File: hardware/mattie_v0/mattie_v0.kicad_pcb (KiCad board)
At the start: 4 copper layers, 55 x 32 mm, 53 parts, among them J1 5V, J2 USB_B_Mini, J3 Power, U1 STM32F40X_LQFP64, U2 ICE40UP5K-SG48ITR, U3 MCP1826T, U4 MCP1826S-3302, U5 DSC1004, Y1 8Mhz

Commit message: adding some cap
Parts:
- added C26: 0.1u, Capacitor_SMD:C_0603_1608Metric, F.Cu at (146.9, 124.0)
- 5 - 6V: renamed from J1
- renumbered BOOT_MODE to SW1
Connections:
- net /MCU/ADC12_IN8 renamed Net-(U1-Pad26)
- net /MCU/ADC12_IN9 renamed Net-(U1-Pad27)
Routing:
- net +1V2: track 75.2 -> 91.6 mm
- net GND: track 453.9 -> 450.6 mm

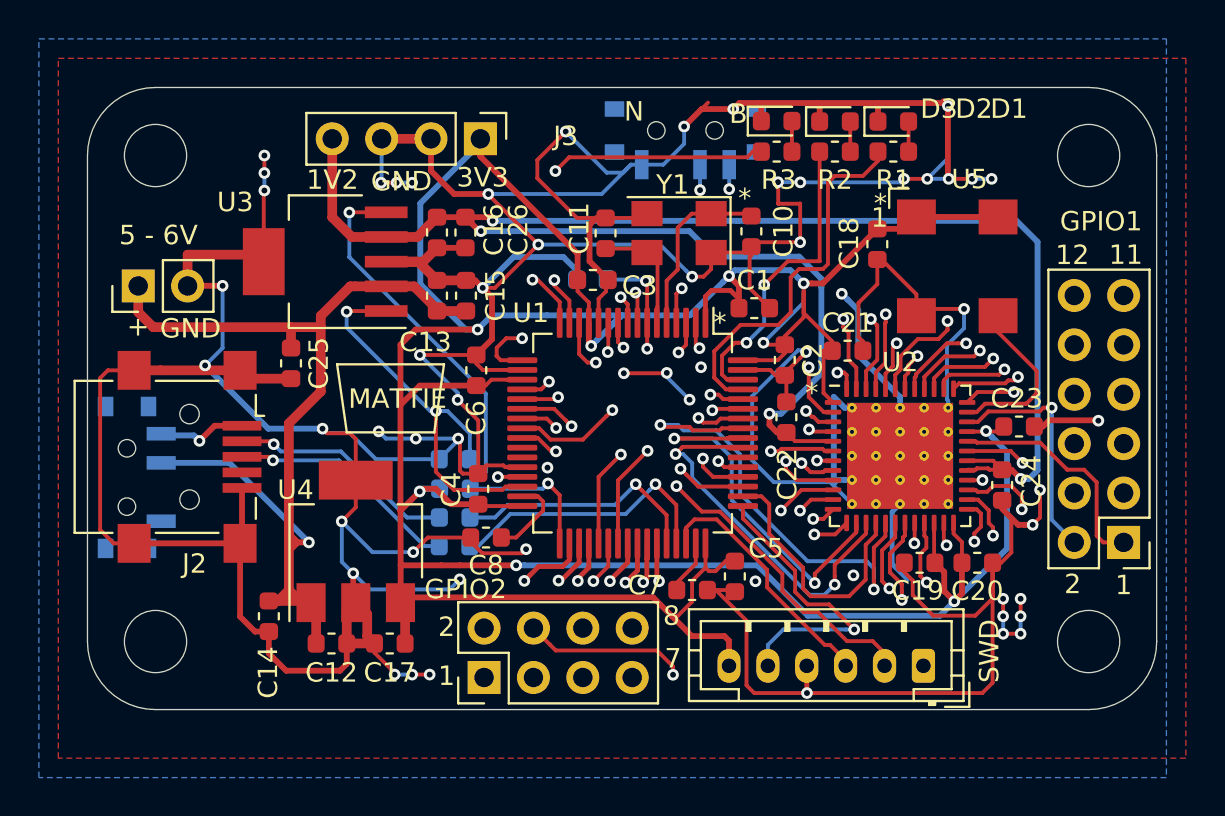
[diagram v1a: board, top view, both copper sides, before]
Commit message: added pullups and pulldowns
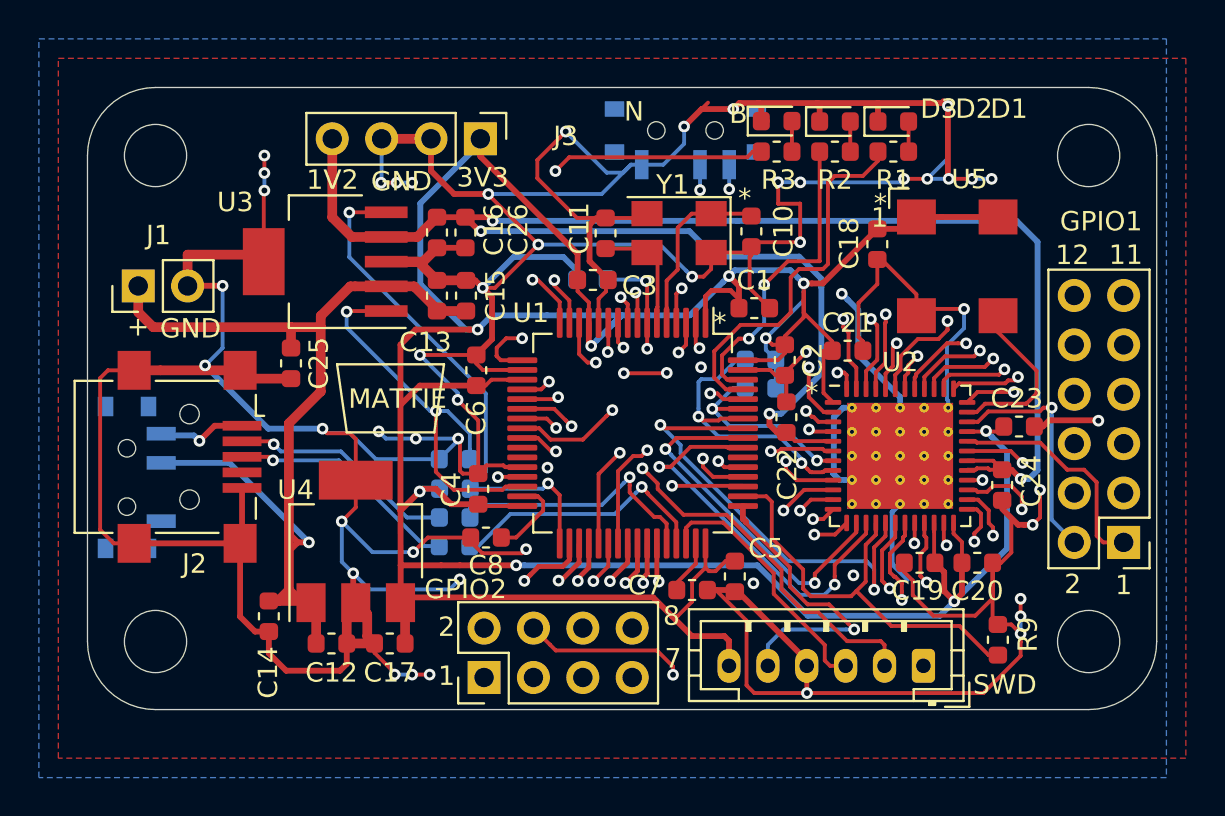
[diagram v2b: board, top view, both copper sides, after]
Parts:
- added R10: 10K, Resistor_SMD:R_0603_1608Metric, B.Cu at (162.1, 132.0)
- added R6: 10K, Resistor_SMD:R_0603_1608Metric, B.Cu at (162.1, 130.5)
- added R9: 10K, Resistor_SMD:R_0603_1608Metric, F.Cu at (174.3, 144.9)
- J1: renamed from 5 - 6V
- renumbered SW1 to BOOT_MODE
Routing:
- net GND: track 450.6 -> 439.9 mm, vias 55 -> 51
- net /LATTICE_ICE40/SPI_SS: track 13.5 -> 22.3 mm
- net /LATTICE_ICE40/RESET: track 10.7 -> 15.5 mm
- net +3V3: track 200.6 -> 203.1 mm
- net /LATTICE_ICE40/DONE: track 8.89 -> 11.0 mm
- net /LATTICE_ICE40/SPI_SCK: track 19.3 -> 20.6 mm
- net /LATTICE_ICE40/SPI_MOSI: track 24.4 -> 23.4 mm
- net Net-(R4-Pad1): track 12.9 -> 13.7 mm
- net Net-(R5-Pad1): track 14.4 -> 13.7 mm
- net /MCU/NRST: track 29.6 -> 30.2 mm
- net /MCU/SWCLK: track 15.4 -> 15.9 mm
- net /LATTICE_ICE40/DAT7: track 26.6 -> 26.1 mm

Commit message: Changed some cap values and added extra caps
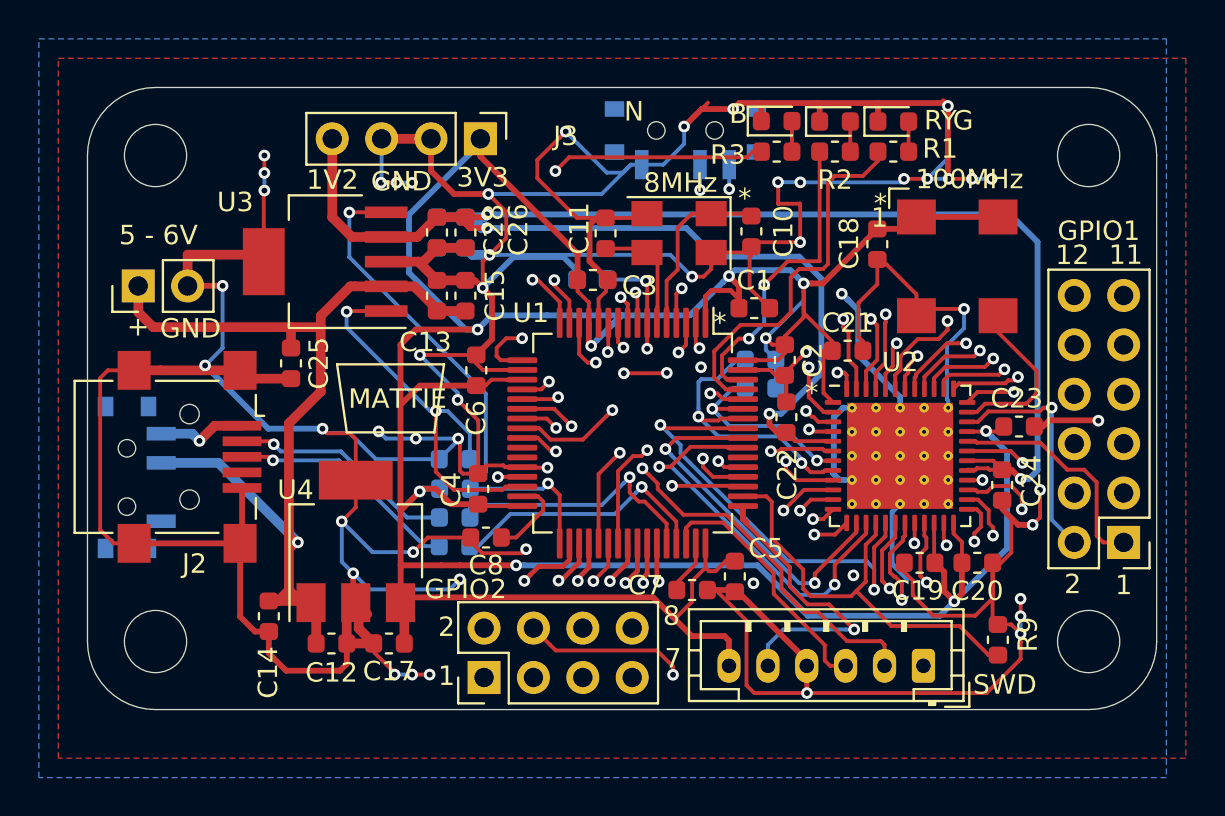
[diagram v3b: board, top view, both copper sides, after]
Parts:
- added C27: 4.7u, Capacitor_SMD:C_0603_1608Metric, B.Cu at (145.5, 124.0)
- added C28: 4.7u, Capacitor_SMD:C_0603_1608Metric, F.Cu at (145.5, 124.0)
- 5 - 6V: renamed from J1
- C16: value 2.2u -> 4.7u; moved to B.Cu
- C17: value 2.2u -> 4.7u
- moved C16 1.46 mm to (146.9, 124.0)
- renumbered U5 to 100MHz, Y1 to 8MHz, D1 to G, D3 to R, D2 to Y
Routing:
- net GND: track 439.9 -> 444.5 mm
- net +1V2: track 91.6 -> 96.1 mm
- net /DCDC/5V_IN: track 55.9 -> 54.7 mm
- net +3V3: track 203.1 -> 203.9 mm

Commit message: flash yellow led if reset of FPGA is ok
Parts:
- U1: value STM32F40X_LQFP64 -> STM32
- U2: value ICE40UP5K-SG48ITR -> ICE40

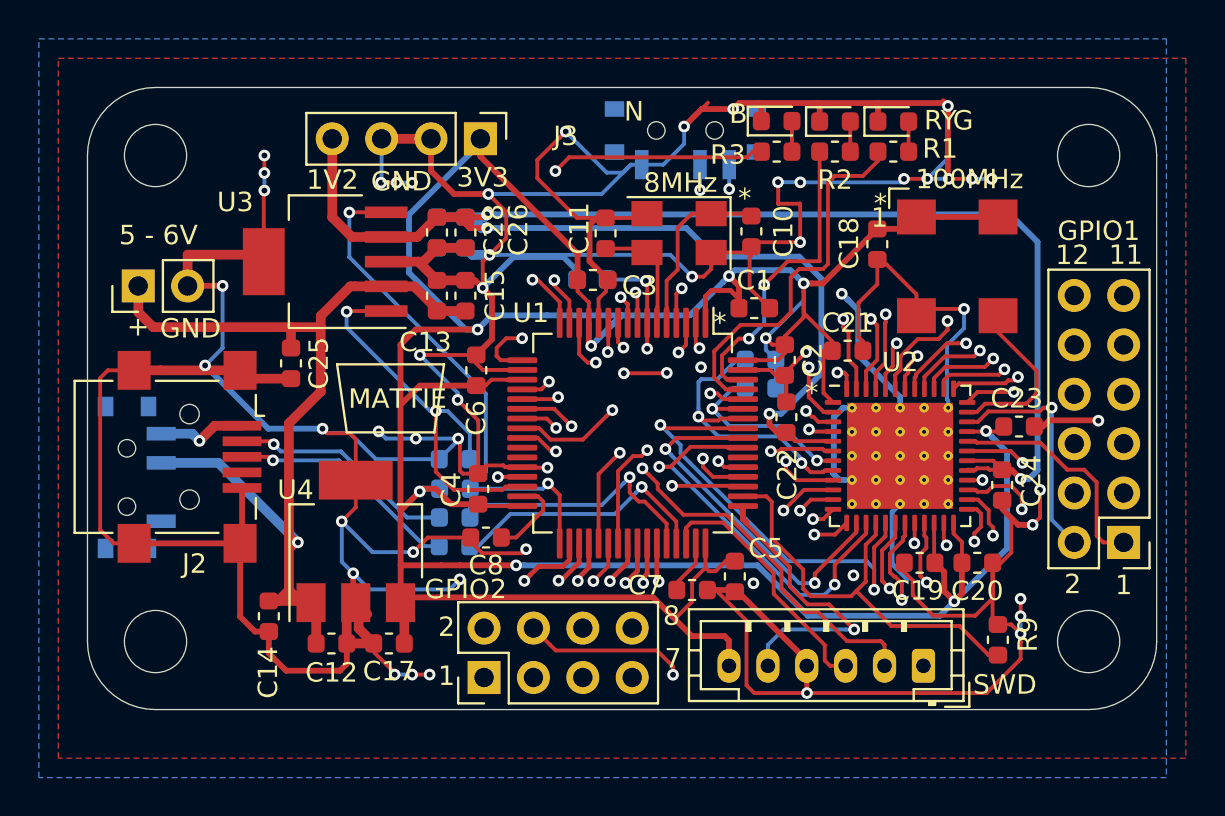
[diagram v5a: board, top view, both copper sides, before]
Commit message: restored kicad_pcb from old commit
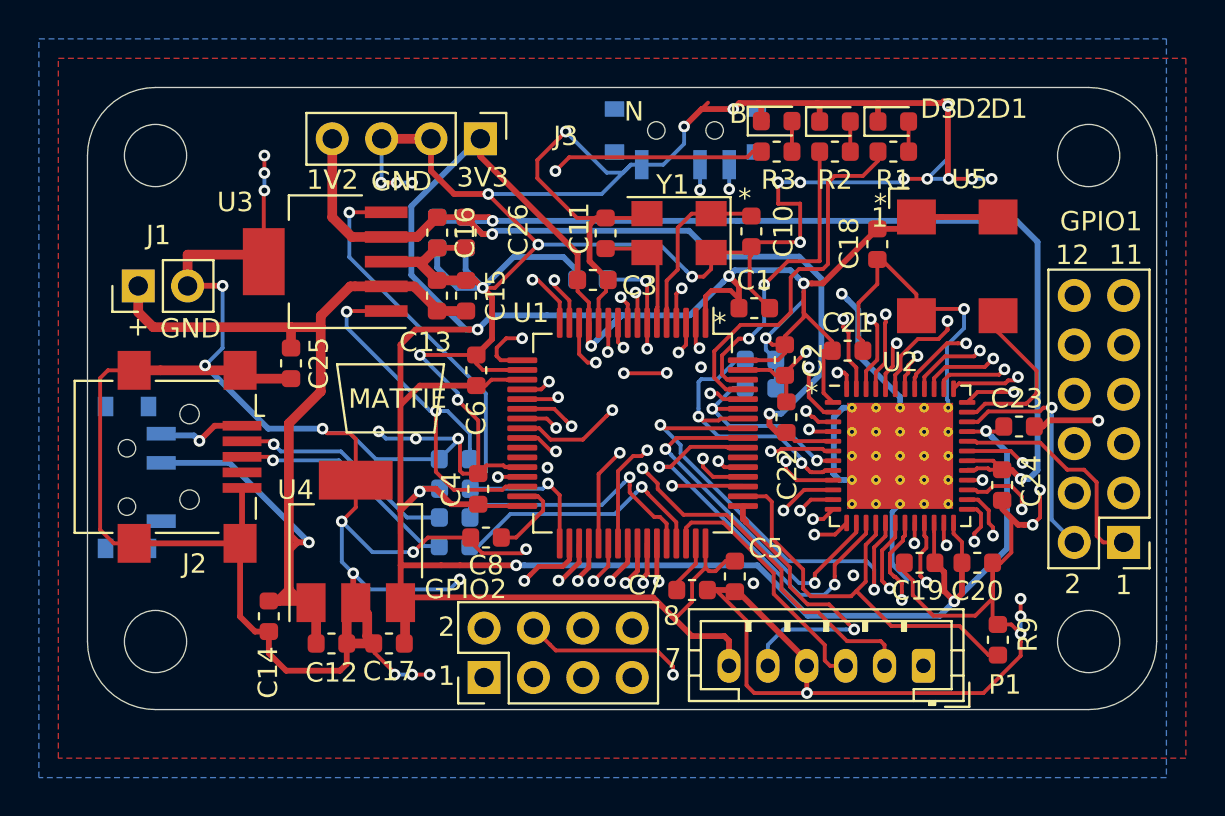
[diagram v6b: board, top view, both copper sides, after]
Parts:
- C16: moved to F.Cu
- C28: moved to B.Cu
- J1: renamed from 5 - 6V
- U1: value STM32 -> STM32F40X_LQFP64
- U2: value ICE40 -> ICE40UP5K-SG48ITR
- moved C28 1.47 mm to (146.9, 124.0)
- moved C16 1.45 mm to (145.5, 124.0)
- renumbered G to D1, Y to D2, R to D3, SWD to P1, BOOT_MODE to SW1, USB_POWER to SW2, 100MHz to U5, 8MHz to Y1
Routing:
- net +1V2: track 96.1 -> 97.9 mm
- net GND: track 444.5 -> 446.1 mm
- net /DCDC/5V_IN: track 54.7 -> 55.9 mm
